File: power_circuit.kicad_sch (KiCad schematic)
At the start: 11 parts, among them U1 L7812, U2 L7805

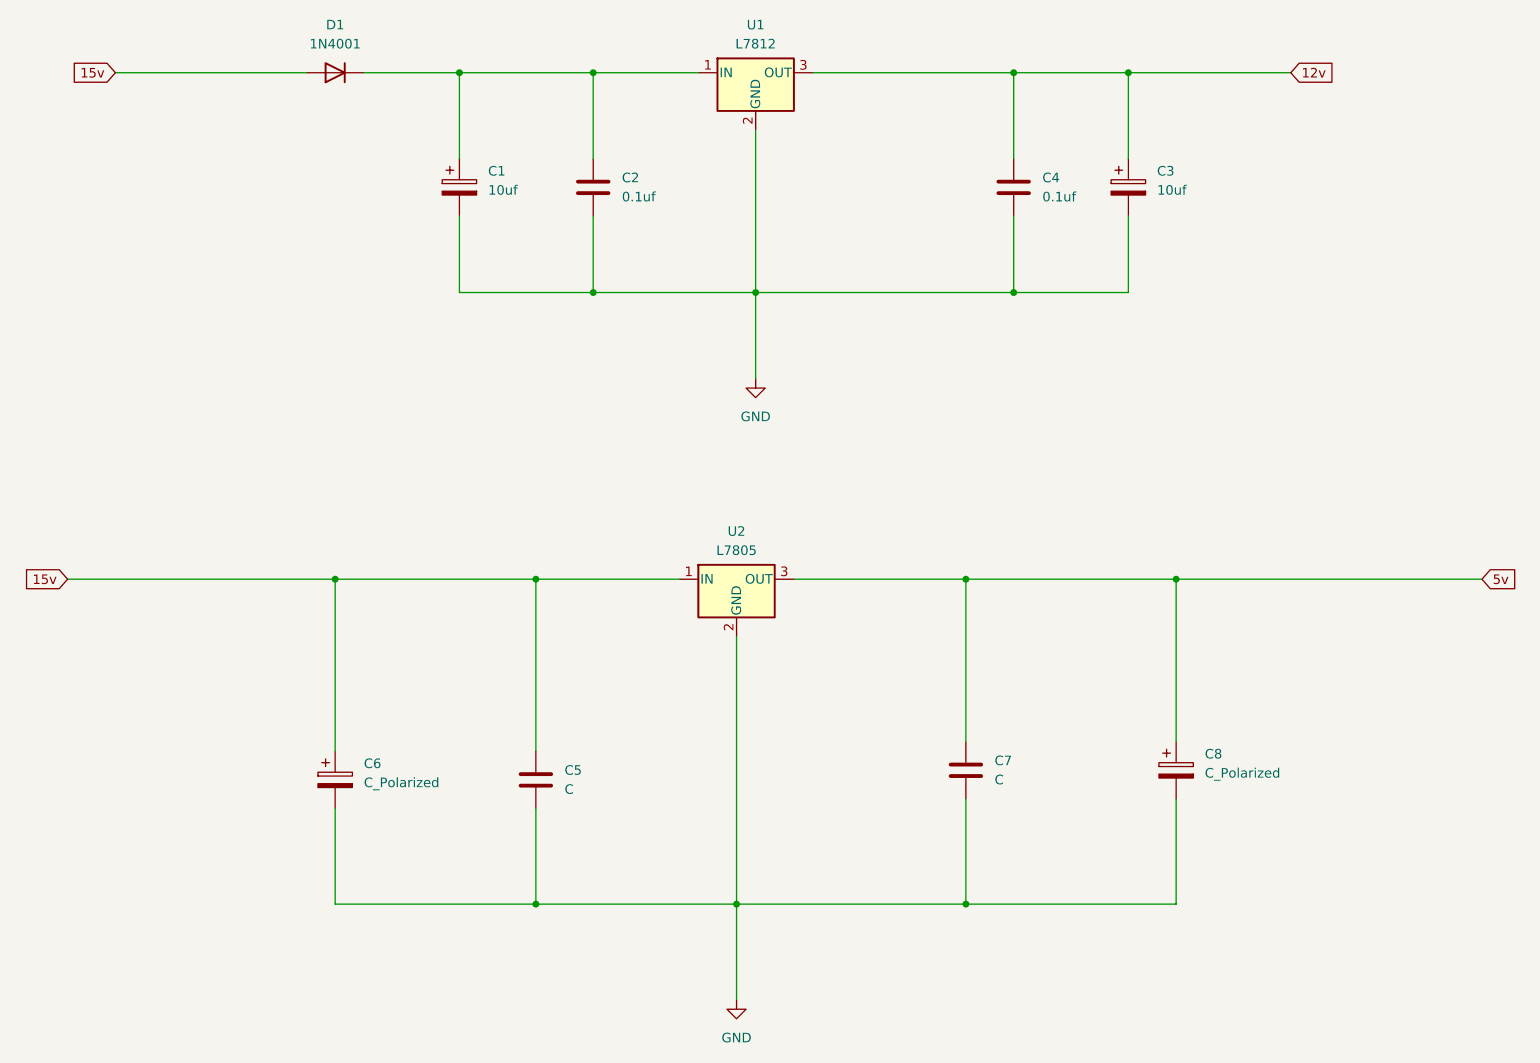
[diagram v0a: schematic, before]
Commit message: added label on the capacitors and added diode to the 5v regulator for reverse polarity
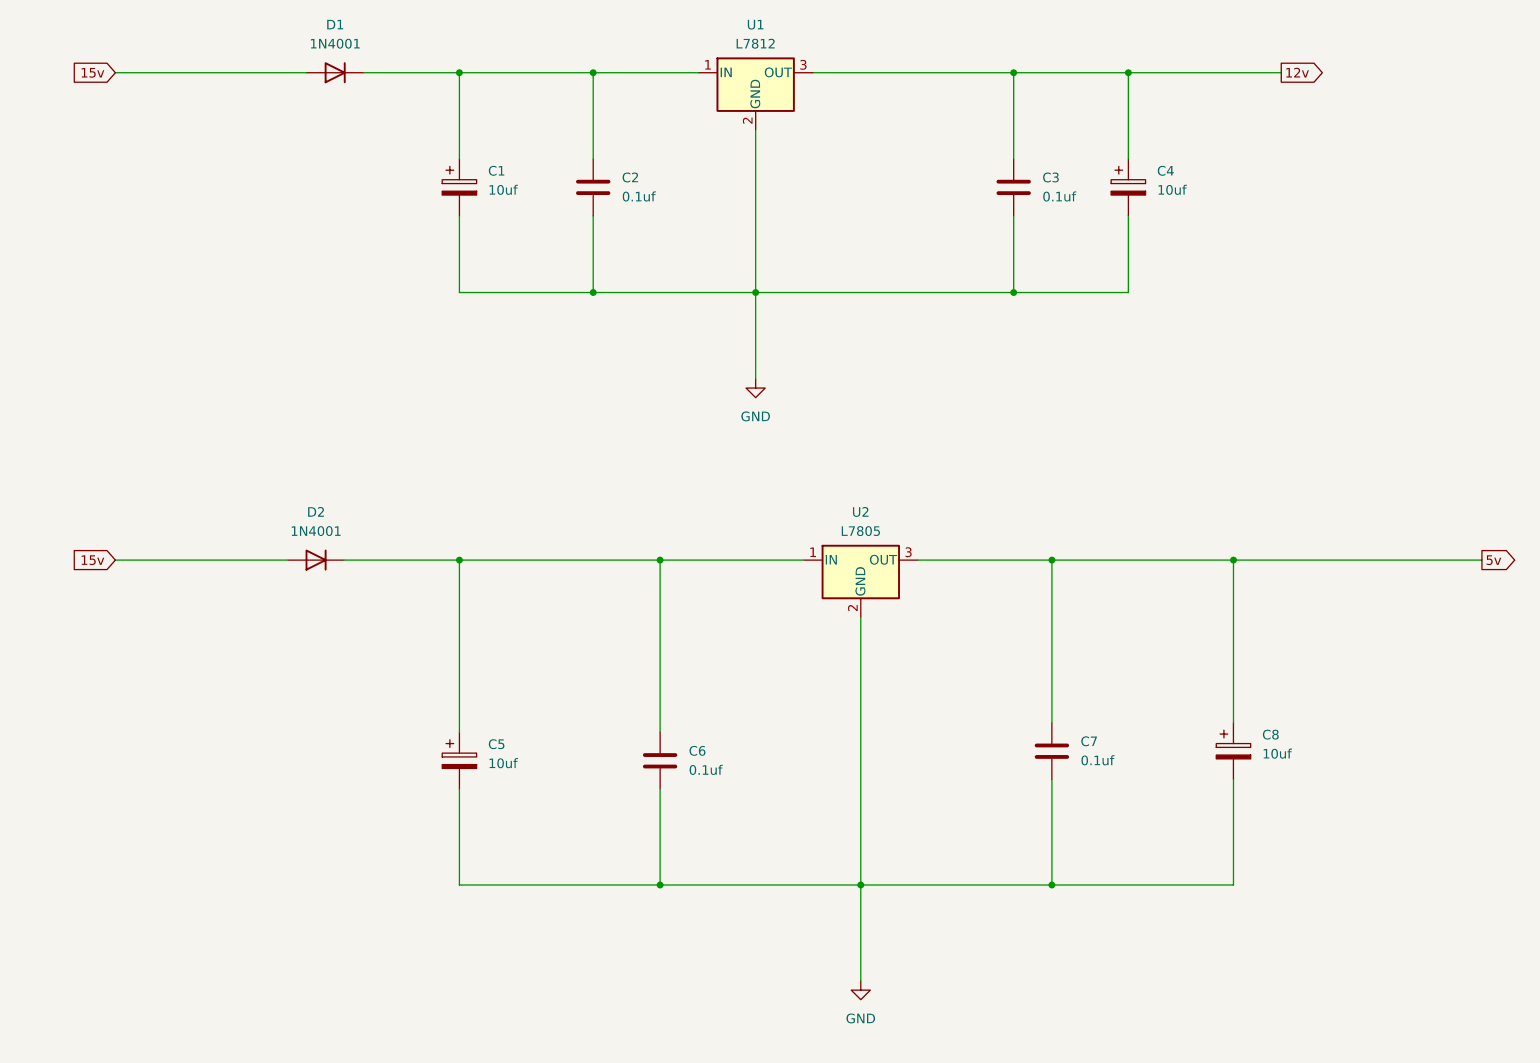
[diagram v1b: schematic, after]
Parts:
- added D2: 1N4001, Diode_THT:D_DO-41_SOD81_P10.16mm_Horizontal, symbol Diode:1N4001
- C5: renamed from C6; value C_Polarized -> 10uf
- C6: renamed from C5; value C -> 0.1uf
- C7: value C -> 0.1uf
- C8: value C_Polarized -> 10uf
- renumbered C4 to C3, C3 to C4
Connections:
- net 15v: now also D2.2 (A); no longer C5.1, C6.1, U2.1 (IN)
- new net: C5.1, C6.1, D2.1 (K), U2.1 (IN)
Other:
- moved on the sheet: C5, C6, C7, C8, U2
